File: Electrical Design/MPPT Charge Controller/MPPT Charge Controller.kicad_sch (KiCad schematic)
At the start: 67 parts, among them J1 Conn_01x02_Socket, J2 Conn_01x02_Socket, J3 Conn_01x02_Socket, Q1 Q_Dual_NMOS_S1G1S2G2D2D2D1D1, Q2 Q_Dual_NMOS_S1G1S2G2D2D2D1D1, Q3 2N7002, U2 AP63203WU, U3 ACS712xLCTR-05B, U4 ACS712

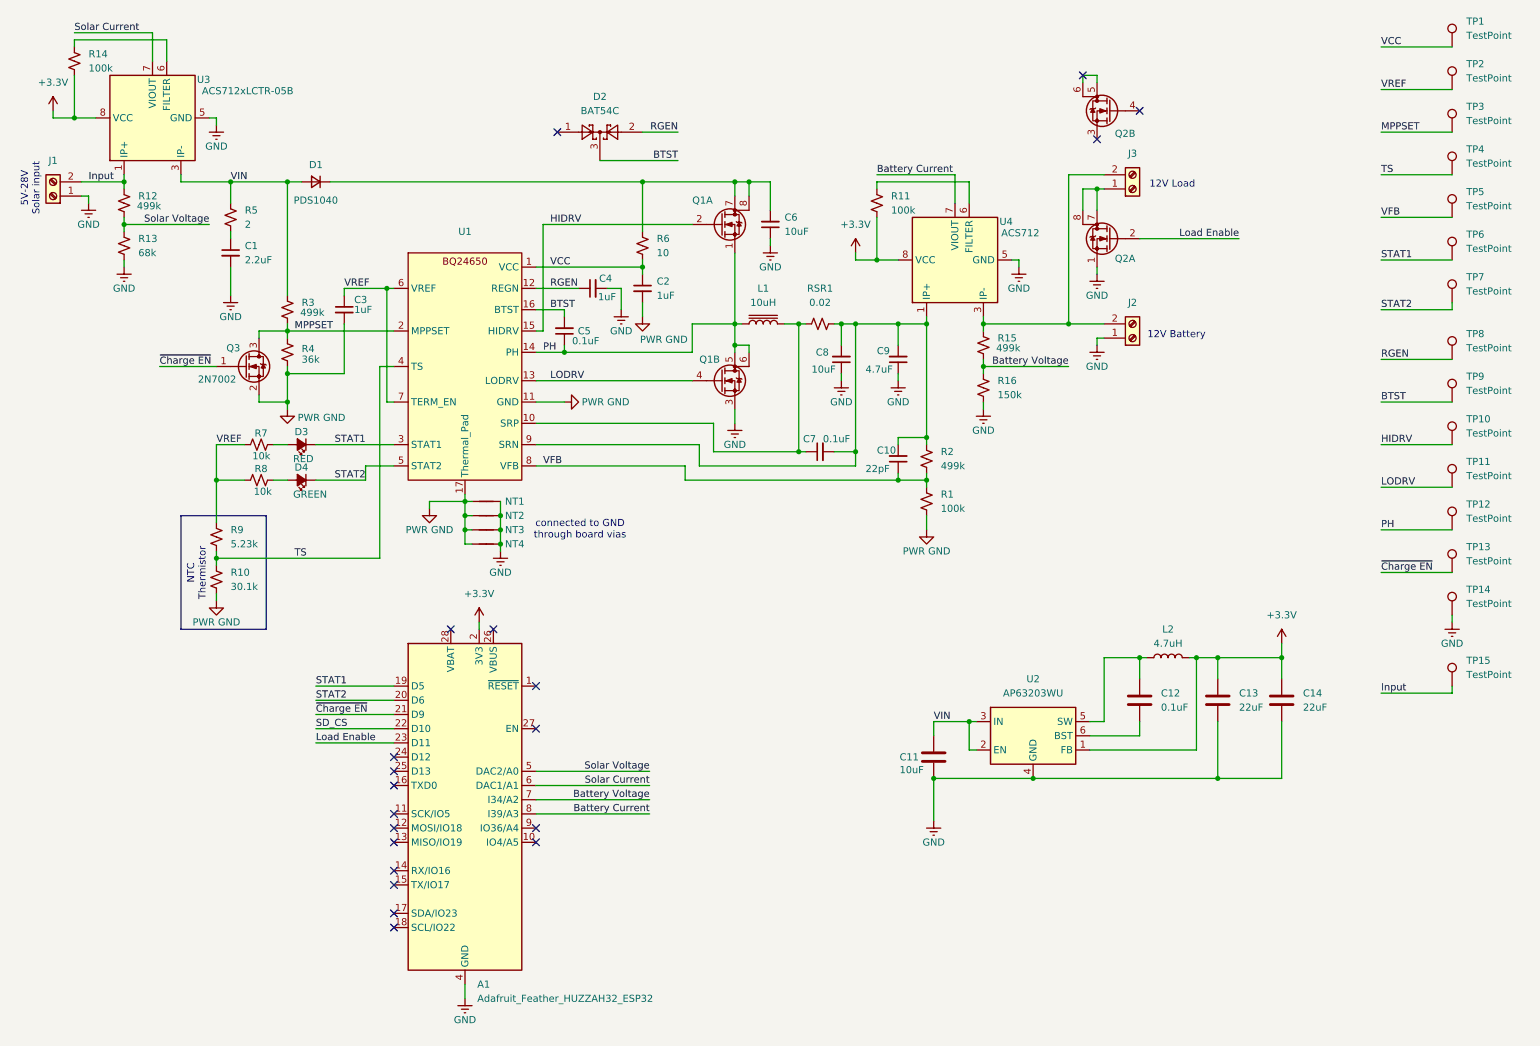
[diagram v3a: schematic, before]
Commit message: fixed R4 inconsistency
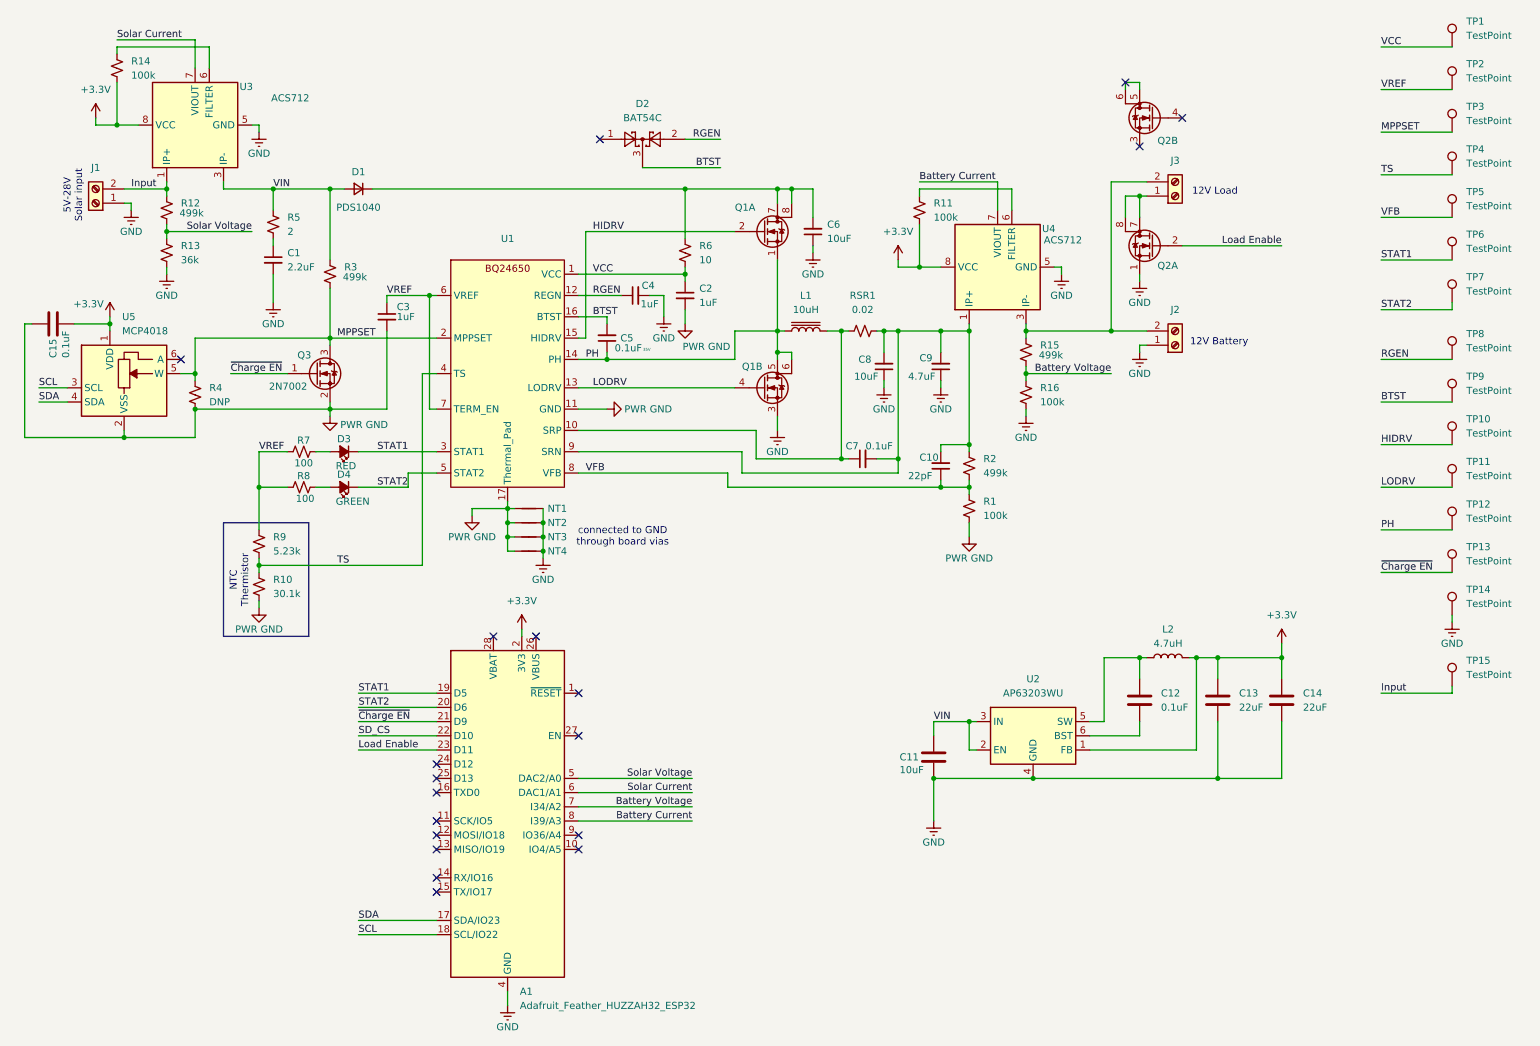
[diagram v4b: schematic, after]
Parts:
- added C15: 0.1uF, Capacitor_SMD:C_0603_1608Metric, symbol Device:C
- added U5: MCP4018, Package_TO_SOT_SMD:SOT-363_SC-70-6, symbol Potentiometer_Digital:MCP4018-xxxxLT
- C5: Voltage Rating (none) -> 35V
- R13: value 68k -> 36k
- R16: value 150k -> 100k
- R4: value 36k -> DNP
- R7, R8: value 10k -> 100
- U3: value ACS712xLCTR-05B -> ACS712
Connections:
- net +3.3V: now also C15.1, U5.1 (VDD)
- net MPPSET: now also U5.5 (W)
- net PWR GND: now also C15.2, U5.2 (VSS)
- net SDA: now reaches A1.17 (SDA/IO23)
- net SDA: now also U5.4 (SDA)
- net SCL: now reaches A1.18 (SCL/IO22)
- net SCL: now also U5.3 (SCL)
- no-connect marks 20 -> 19
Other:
- title: (none) -> MPPT Charge Controller
- moved on the sheet: A1, C1, C10, C2, C3, C4, C5, C6, C7, C8, C9, D1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

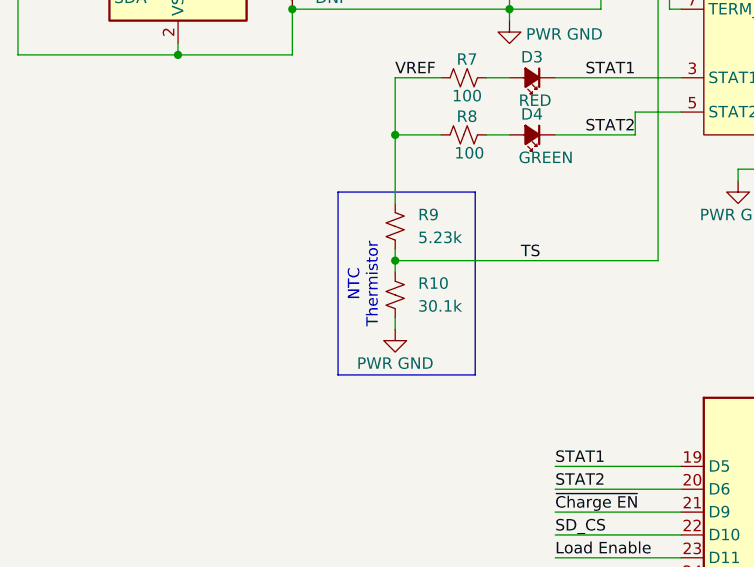
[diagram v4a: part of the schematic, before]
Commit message: Added battery temp thermistor connector
Also cleaned up directory and added .gitignore
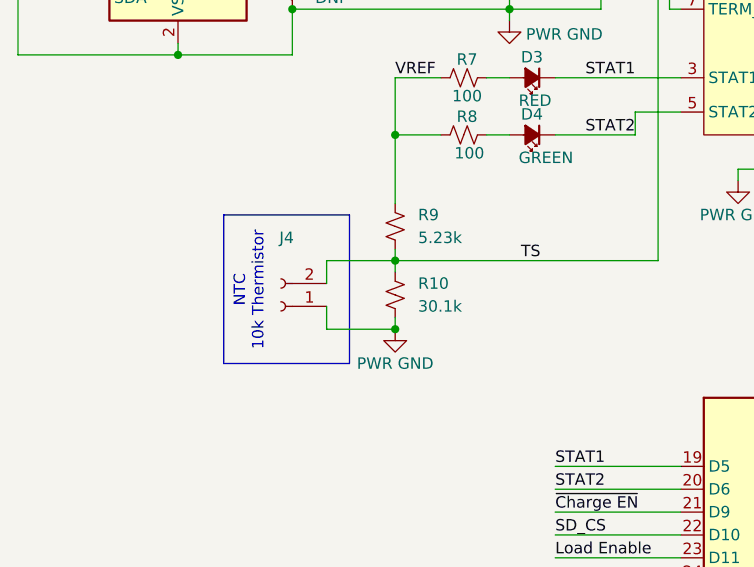
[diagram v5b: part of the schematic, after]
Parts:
- added J4: ~, Connector_PinSocket_2.54mm:PinSocket_1x02_P2.54mm_Vertical, symbol Connector:Conn_01x02_Socket
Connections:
- net PWR GND: now also J4.1 (Pin_1)
- net TS: now also J4.2 (Pin_2)
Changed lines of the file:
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@@
 	(title_block
 		(title "MPPT Charge Controller")
-		(rev "0.2")
+		(rev "0.3")
 	)
 	(junction
@@
 	)
 	(junction
+		(at 57.15 120.65)
+		(diameter 0)
+		(color 0 0 0 0)
+	)
+	(junction
 		(at 184.15 99.06)
 		(diameter 0)
@@
 	(wire
 		(pts
+			(xy 49.53 113.03) (xy 49.53 115.57)
+		)
+		(stroke
+			(width 0)
+			(type default)
+		)
+	)
+	(wire
+		(pts
 			(xy 74.93 146.05) (xy 88.9 146.05)
 		)
@@
 	(wire
 		(pts
+			(xy 49.53 120.65) (xy 57.15 120.65)
+		)
+		(stroke
+			(width 0)
+			(type default)
+		)
+	)
+	(wire
+		(pts
 			(xy 168.91 71.12) (xy 168.91 74.93)
 		)
@@
 	(wire
 		(pts
+			(xy 49.53 118.11) (xy 49.53 120.65)
+		)
+		(stroke
+			(width 0)
+			(type default)
+		)
+	)
+	(wire
+		(pts
 			(xy 161.29 71.12) (xy 158.75 71.12)
 		)
@@
 	(wire
 		(pts
+			(xy 57.15 113.03) (xy 49.53 113.03)
+		)
+		(stroke
+			(width 0)
+			(type default)
+		)
+	)
+	(wire
+		(pts
 			(xy 115.57 53.34) (xy 142.24 53.34)
 		)
@@
 		)
 	)
-	(text_box "NTC\nThermistor"
+	(text_box "NTC\n10k Thermistor"
 		(exclude_from_sim no)
-		(at 50.8 105.41 90)
-		(size 15.24 20.32)
+		(at 38.1 107.95 90)
+		(size 13.97 16.51)
 		(stroke
 			(width 0)
@@
 					(unit 1)
 				)
+			)
+		)
+	)
+	(symbol
+		(lib_id "Connector:Conn_01x02_Socket")
+		(at 44.45 118.11 180)
+		(unit 1)
+		(exclude_from_sim no)
+		(in_bom yes)
+		(on_board yes)
+		(dnp no)
+		(property "Reference" "J4"
+			(at 45.085 110.49 0)
+			(effects
+				(font
+					(size 1.27 1.27)
+				)
+			)
+		)
+		(property "Value" "~"
+			(at 44.45 128.016 0)
+			(effects
+				(font
+					(size 1.27 1.27)
+				)
+			)
+		)
+		(property "Footprint" "Connector_PinSocket_2.54mm:PinSocket_1x02_P2.54mm_Vertical"
+			(at 44.45 118.11 0)
+			(effects
+				(font
+					(size 1.27 1.27)
+				)
+				(hide yes)
+			)
+		)
+		(property "Datasheet" "~"
+			(at 44.45 118.11 0)
+			(effects
+				(font
+					(size 1.27 1.27)
+				)
+				(hide yes)
+			)
+		)
+		(property "Description" "Generic connector, single row, 01x02, script generated"
+			(at 44.45 118.11 0)
+			(effects
+				(font
+					(size 1.27 1.27)
+				)
+				(hide yes)
+			)
+		)
+		(pin "1"
+		)
+		(pin "2"
+		)
+		(instances
+			(project "MPPT Charge Controller"
+				(path "/6fccb5b0-46ff-4014-9169-aa61e4064f3f"
+					(reference "J4")
+					(unit 1)
+				)
